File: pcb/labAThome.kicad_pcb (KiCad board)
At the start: 2 copper layers, 100 x 100 mm, 57 parts, among them J1 BME280, J10 SRV2, J12 FA2, J13 Barrel_Jack_Switch, J14 FA3, J2 SRV1, J3 5V, J4 EXTENSION, J5 VPS, J9 FA1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

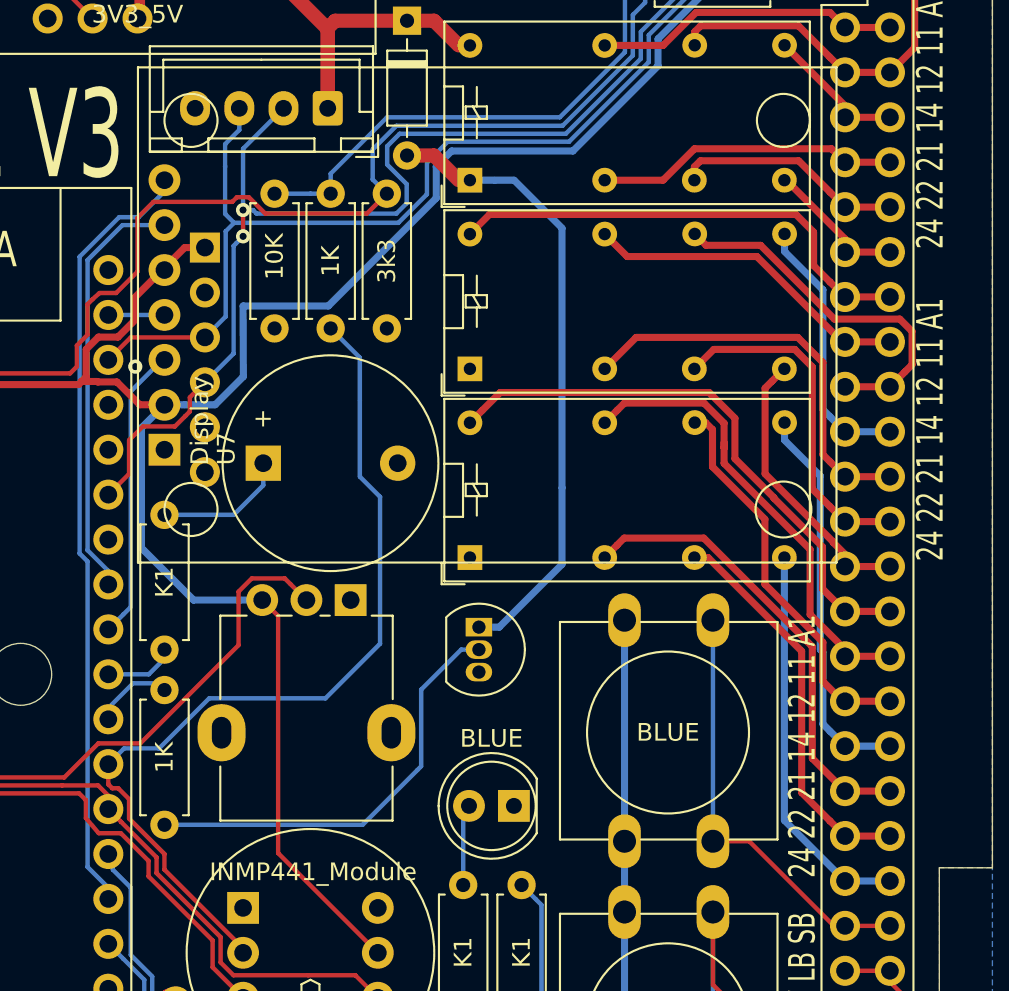
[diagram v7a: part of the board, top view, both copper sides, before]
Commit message: Slight optimizations in PCB
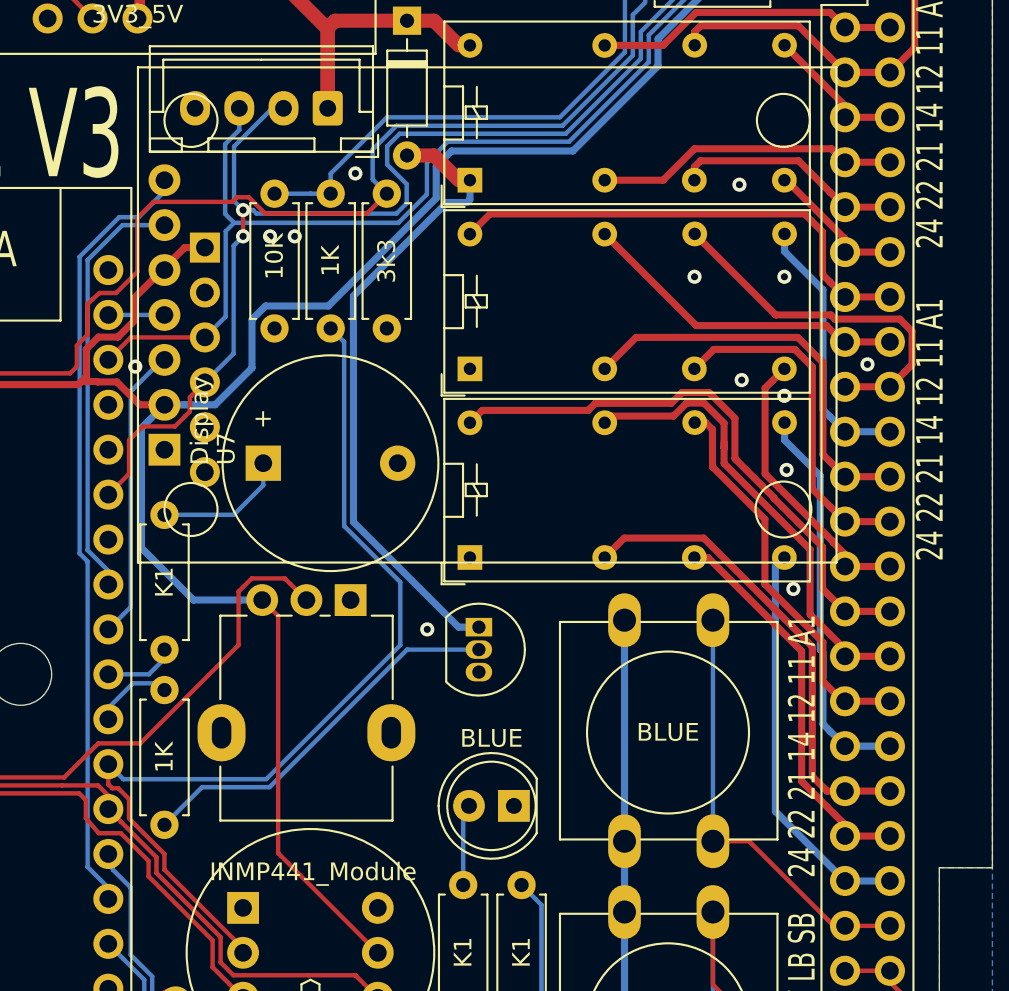
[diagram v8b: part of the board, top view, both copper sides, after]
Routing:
- net Net-(Q4-Pad2): track 24.4 -> 21.9 mm
- net HEATER: track 51.2 -> 53.6 mm
- net SDA: track 67.2 -> 68.0 mm
- net +3V3: track 210.4 -> 209.6 mm
- net R1_21: track 26.2 -> 26.8 mm
- net GND: vias 7 -> 19
